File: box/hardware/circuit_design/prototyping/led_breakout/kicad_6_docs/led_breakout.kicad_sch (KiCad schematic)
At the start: 44 parts, among them J1 rpi_port, U1 MAX6969AWG+, U2 MAX6969AWG+

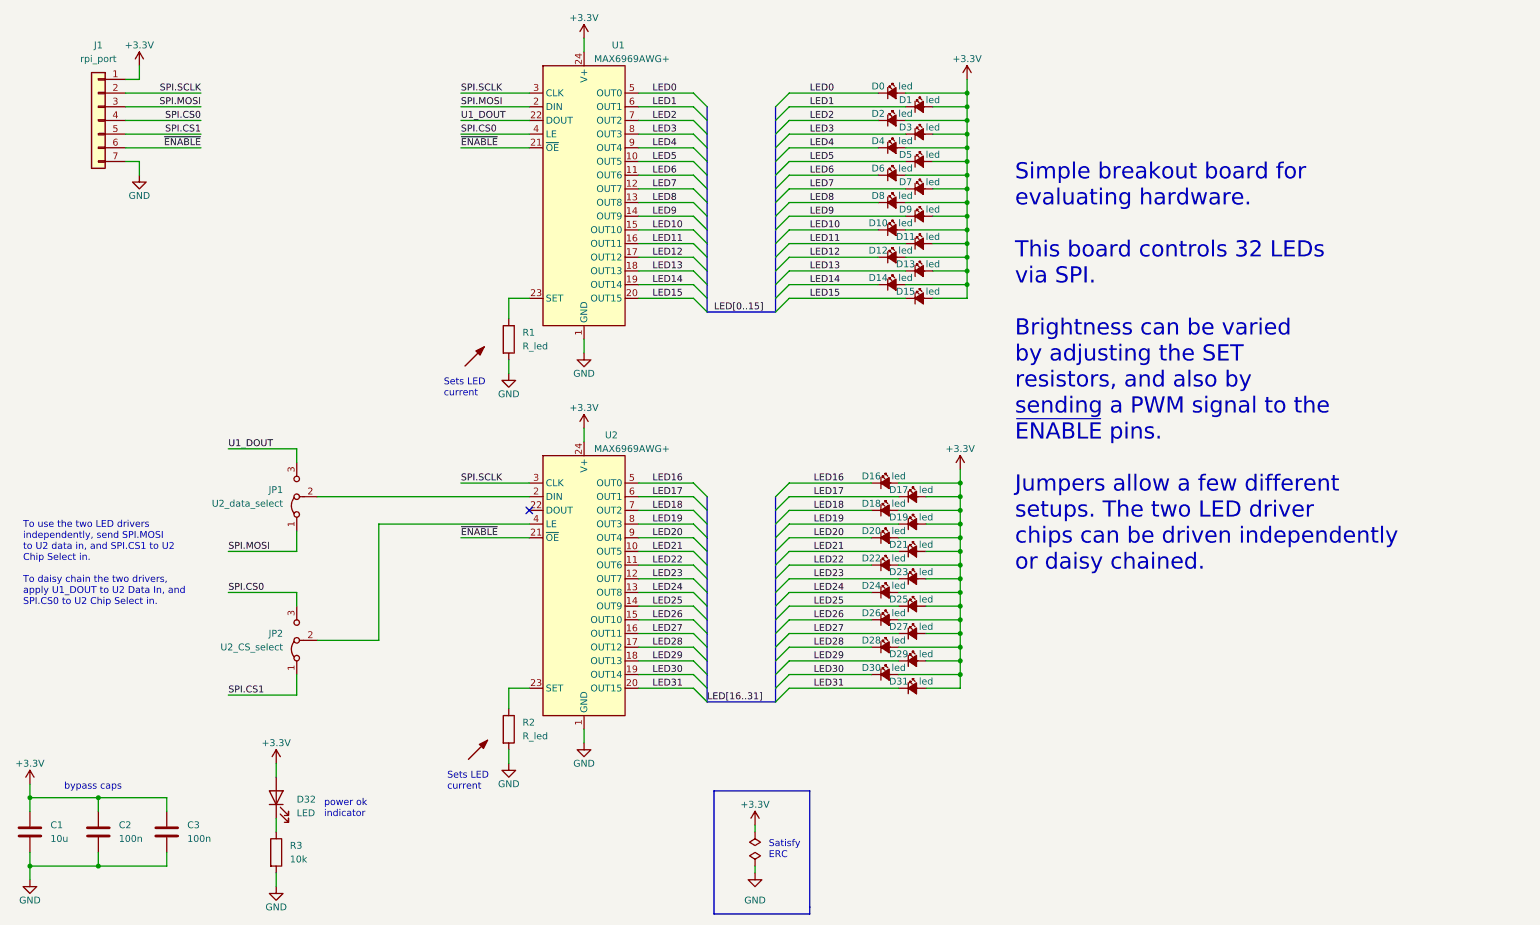
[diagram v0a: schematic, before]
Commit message: Change LED and switch breakouts, use headers instead of components
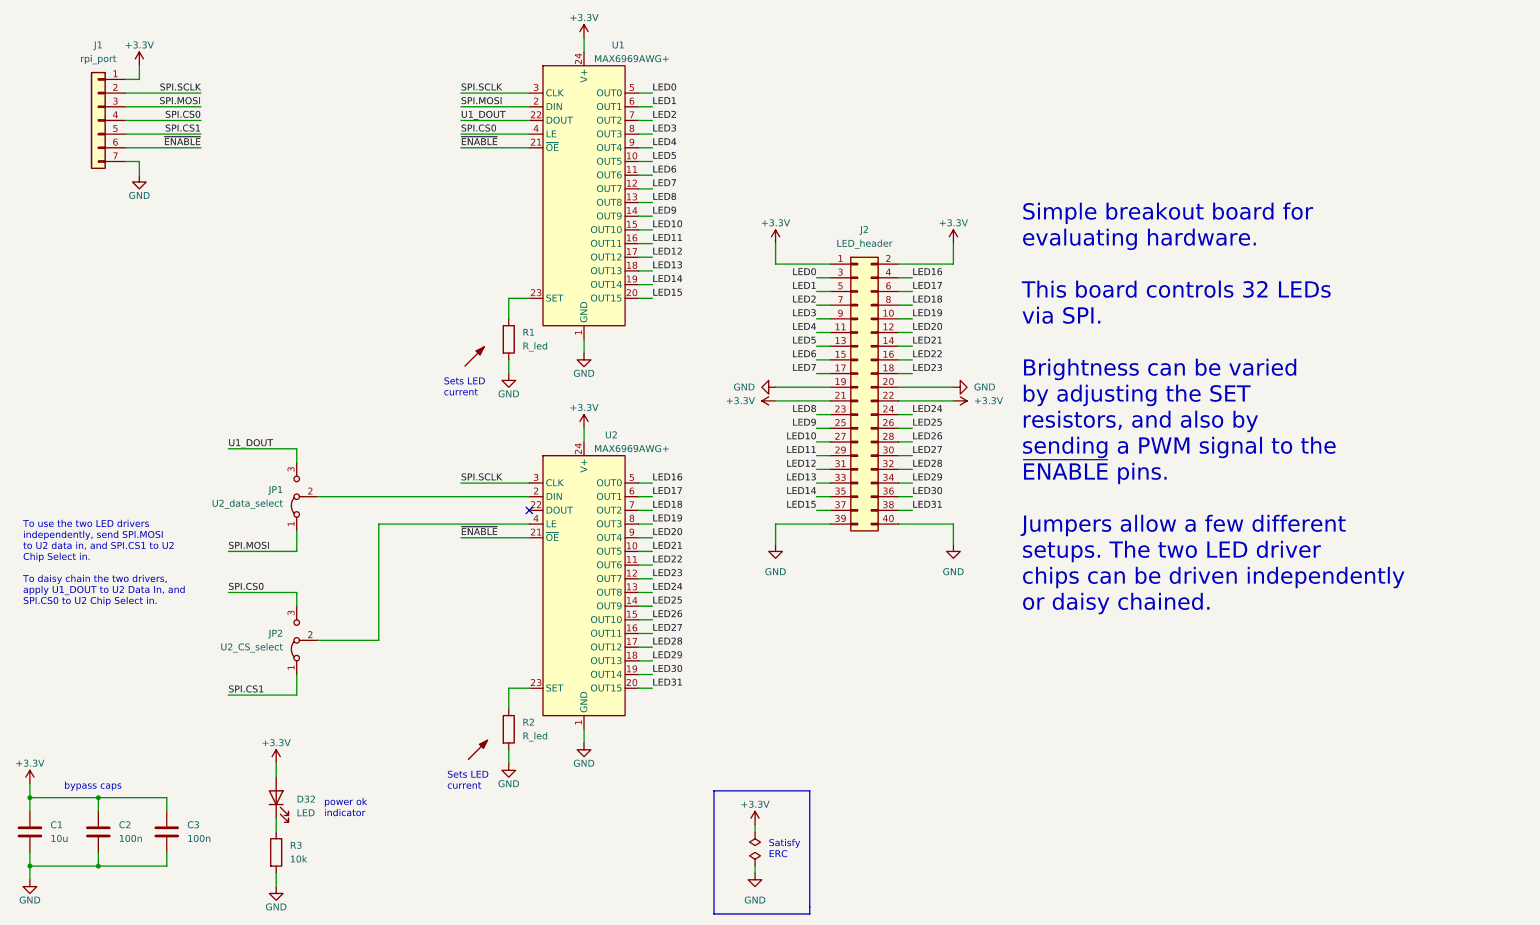
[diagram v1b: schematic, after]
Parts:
- removed D0, D1, D10, D11, D12, D13, D14, D15, D16, D17, D18, D19, D2, D20, D21, D22, D23, D24, D25, D26, D27, D28, D29, D3, D30, D31, D4, D5, D6, D7, D8, D9: led, LED_SMD:LED_0805_2012Metric, symbol Device:LED_Small_Filled
- added J2: LED_header, Connector_PinHeader_2.54mm:PinHeader_2x20_P2.54mm_Vertical, symbol Connector_Generic:Conn_02x20_Odd_Even
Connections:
- net +3V3: now also J2.1 (Pin_1), J2.2 (Pin_2), J2.21 (Pin_21), J2.22 (Pin_22)
- net GND: now also J2.19 (Pin_19), J2.20 (Pin_20), J2.39 (Pin_39), J2.40 (Pin_40)
- net LED0: now also J2.3 (Pin_3)
- net LED1: now also J2.5 (Pin_5)
- net LED10: now also J2.27 (Pin_27)
- net LED11: now also J2.29 (Pin_29)
- net LED12: now also J2.31 (Pin_31)
- net LED13: now also J2.33 (Pin_33)
- net LED14: now also J2.35 (Pin_35)
- net LED15: now also J2.37 (Pin_37)
- net LED16: now also J2.4 (Pin_4)
- net LED17: now also J2.6 (Pin_6)
- net LED18: now also J2.8 (Pin_8)
- net LED19: now also J2.10 (Pin_10)
- net LED2: now also J2.7 (Pin_7)
- net LED20: now also J2.12 (Pin_12)
- net LED21: now also J2.14 (Pin_14)
- net LED22: now also J2.16 (Pin_16)
- net LED23: now also J2.18 (Pin_18)
- net LED24: now also J2.24 (Pin_24)
- net LED25: now also J2.26 (Pin_26)
- net LED26: now also J2.28 (Pin_28)
- net LED27: now also J2.30 (Pin_30)
- net LED28: now also J2.32 (Pin_32)
- net LED29: now also J2.34 (Pin_34)
- net LED3: now also J2.9 (Pin_9)
- net LED30: now also J2.36 (Pin_36)
- net LED31: now also J2.38 (Pin_38)
- net LED4: now also J2.11 (Pin_11)
- net LED5: now also J2.13 (Pin_13)
- net LED6: now also J2.15 (Pin_15)
- net LED7: now also J2.17 (Pin_17)
- net LED8: now also J2.23 (Pin_23)
- net LED9: now also J2.25 (Pin_25)
